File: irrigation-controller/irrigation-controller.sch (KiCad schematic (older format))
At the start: 12 parts, among them IC1 ATMEGA328-A_CHIPACCURATE, J1 B2B-I2C, P1 CONN_10, Q1 2N7002K, Q2 2N7002K, Q3 2N7002K, Q4 2N7002K

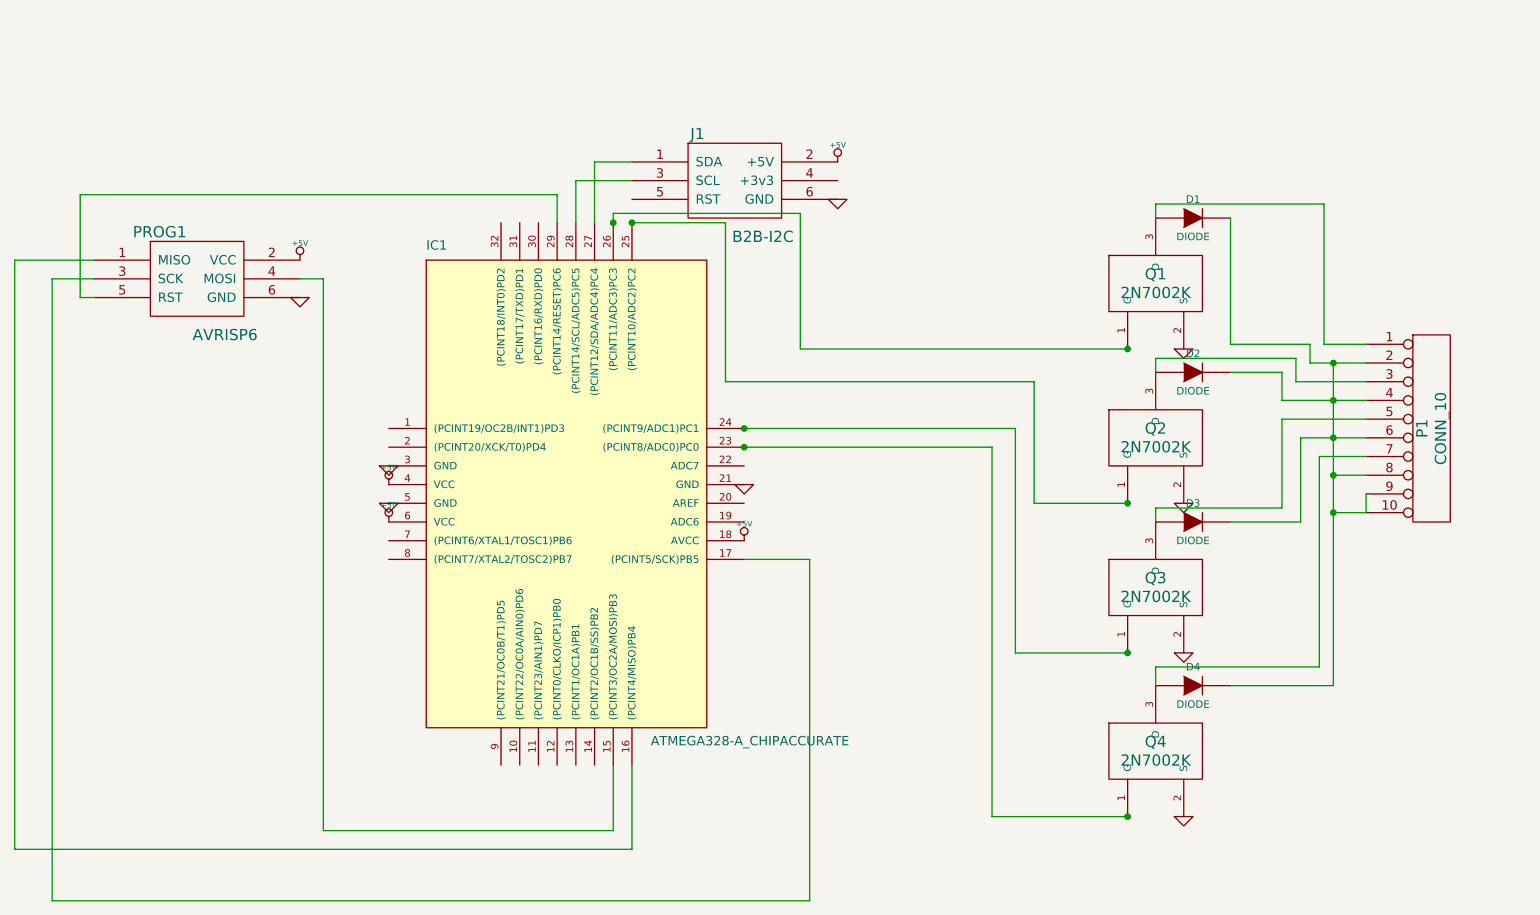
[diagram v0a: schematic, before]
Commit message: Add updated irrigation controller
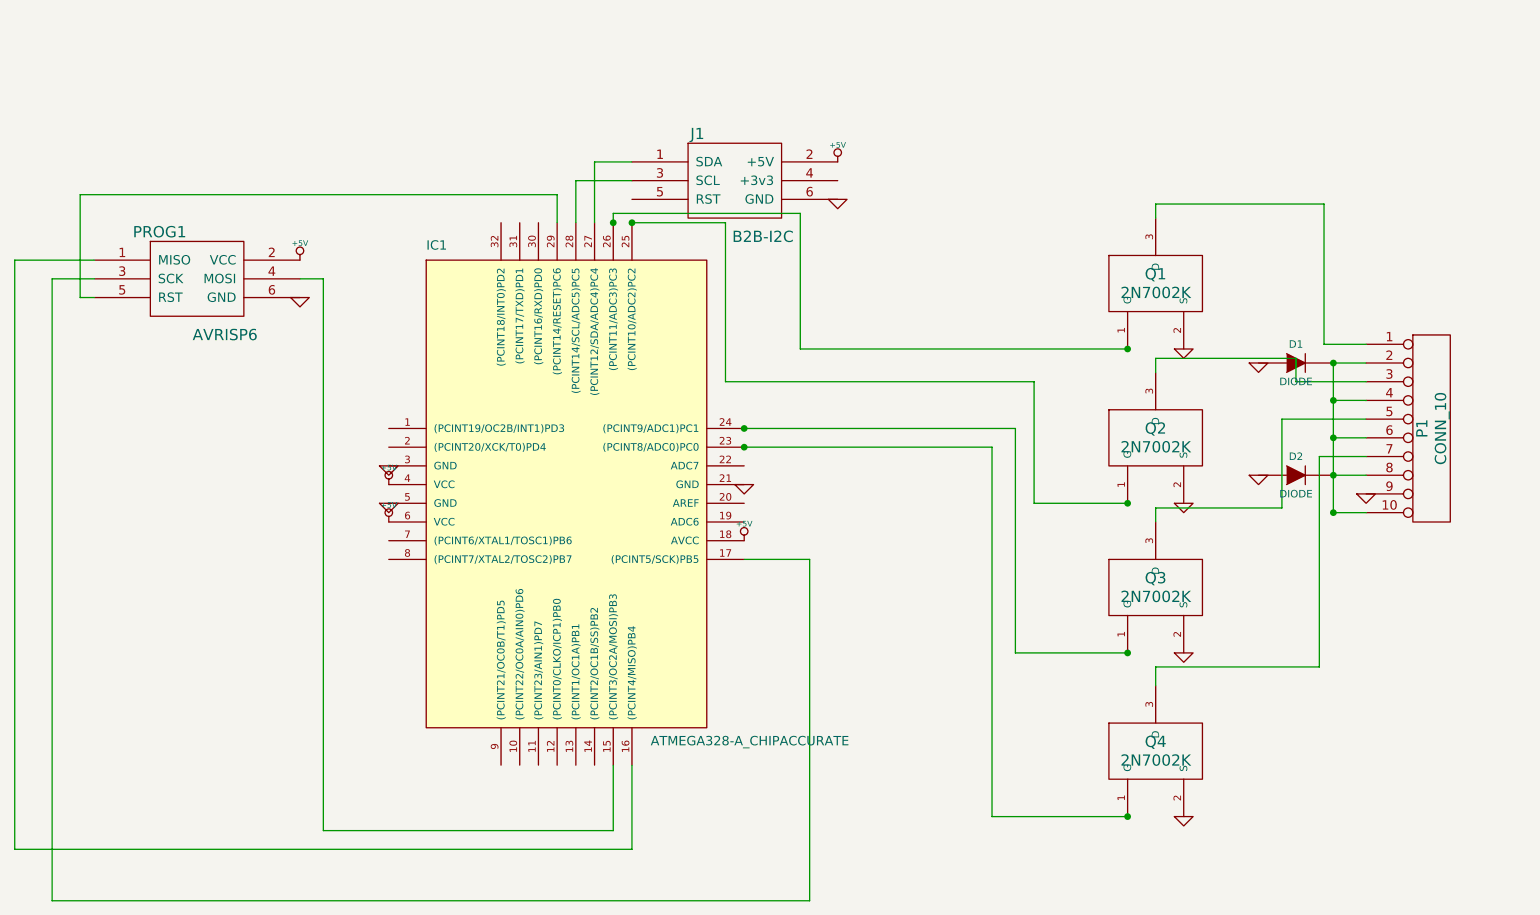
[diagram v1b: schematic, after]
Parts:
- removed D2, D3: DIODE, symbol DIODE
- renumbered D4 to D2
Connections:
- net GND: now also D1.1 (A), D2.1 (A), P1.9 (P9)
- net at P1.1 (P1), Q1.3 (D): no longer D1.1 (A)
- net at P1.7 (P7), Q4.3 (D): no longer D2.1 (A)
- net at D1.2 (K), D2.2 (K), P1.10 (P10)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: no longer P1.9 (P9)
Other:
- moved on the sheet: D1, D2

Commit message: Updated irrigation board: use Teensy or standard AVR-PoE board to drive FETs
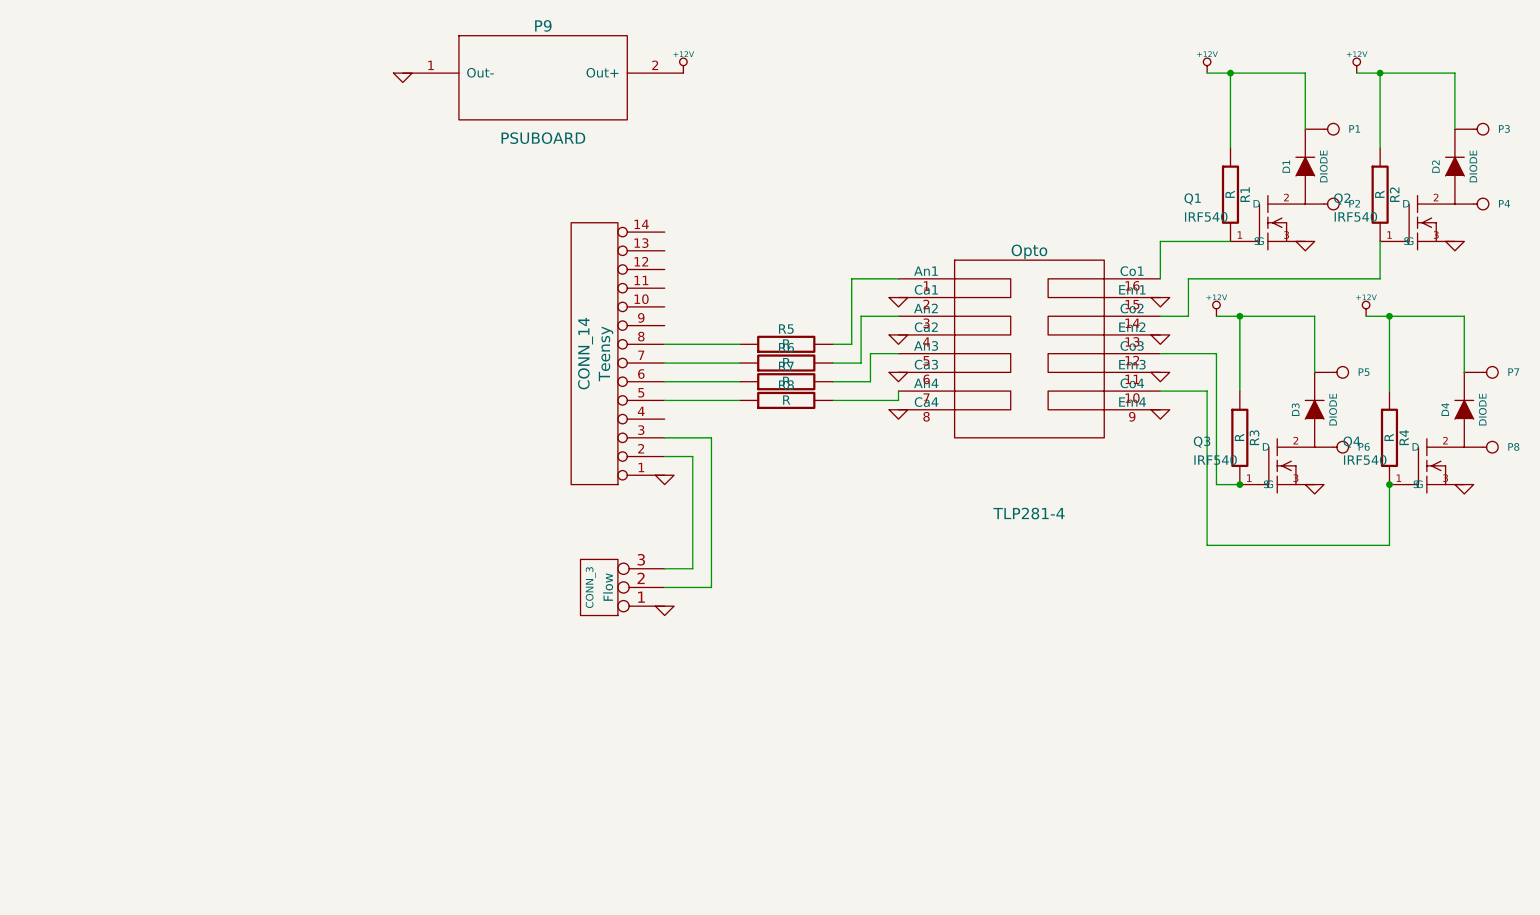
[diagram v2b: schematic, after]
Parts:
- removed IC1: ATMEGA328-A_CHIPACCURATE, TQFP32, symbol ATMEGA328-A_CHIPACCURATE
- removed J1: B2B-I2C, symbol B2B-I2C
- removed P1: CONN_10, symbol CONN_10
- removed PROG1: AVRISP6, symbol AVRISP6
- removed Q1, Q2, Q3, Q4: 2N7002K, symbol 2N7002K
- added D3, D4: DIODE, symbol DIODE
- added Flow: CONN_3, symbol CONN_3
- added Opto: TLP281-4, symbol TLP281-4
- added P1, P2, P3, P4, P5, P6, P7, P8: CONN_1, symbol CONN_1
- added P9: PSUBOARD, symbol PSUBOARD
- added Q1, Q2, Q3, Q4: IRF540, transistor-fet-TO220, symbol IRF540
- added R1, R2, R3, R4, R5, R6, R7, R8: R, symbol R
- added Teensy: CONN_14, symbol CONN_14
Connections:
- net GND: now also Flow.1 (P1), Opto.11 (Em3), Opto.13 (Em2), Opto.15 (Em1), Opto.2 (Ca1), Opto.4 (Ca2), Opto.6 (Ca3), Opto.8 (Ca4), Opto.9 (Em4), P9.1 (Out-), Q1.3 (S), Q2.3 (S), Q3.3 (S), Q4.3 (S), Teensy.1 (P1); no longer D1.1 (A), D2.1 (A)
- net +12V: now reaches D1.2 (K), D2.2 (K)
- net +12V: now also D3.2 (K), D4.2 (K), P1.1, P3.1, P5.1, P7.1, P9.2 (Out+), R1.1, R2.1, R3.1, R4.1
- new net: D1.1 (A), P2.1, Q1.2 (D)
- new net: Opto.16 (Co1), Q1.1 (G), R1.2
- new net: Opto.1 (An1), R5.2
- new net: Opto.10 (Co4), Q4.1 (G), R4.2
- new net: Opto.12 (Co3), Q3.1 (G), R3.2
- new net: Opto.14 (Co2), Q2.1 (G), R2.2
- new net: Opto.3 (An2), R6.2
- new net: Opto.5 (An3), R7.2
- new net: Opto.7 (An4), R8.2
- new net: D2.1 (A), P4.1, Q2.2 (D)
- new net: D4.1 (A), P8.1, Q4.2 (D)
- new net: D3.1 (A), P6.1, Q3.2 (D)
- new net: Flow.3 (P3), Teensy.2 (P2)
- new net: Flow.2 (PM), Teensy.3 (P3)
- new net: R8.1, Teensy.5 (P5)
- new net: R7.1, Teensy.6 (P6)
- new net: R6.1, Teensy.7 (P7)
- new net: R5.1, Teensy.8 (P8)

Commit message: Add power supply switching, and do some cleanup
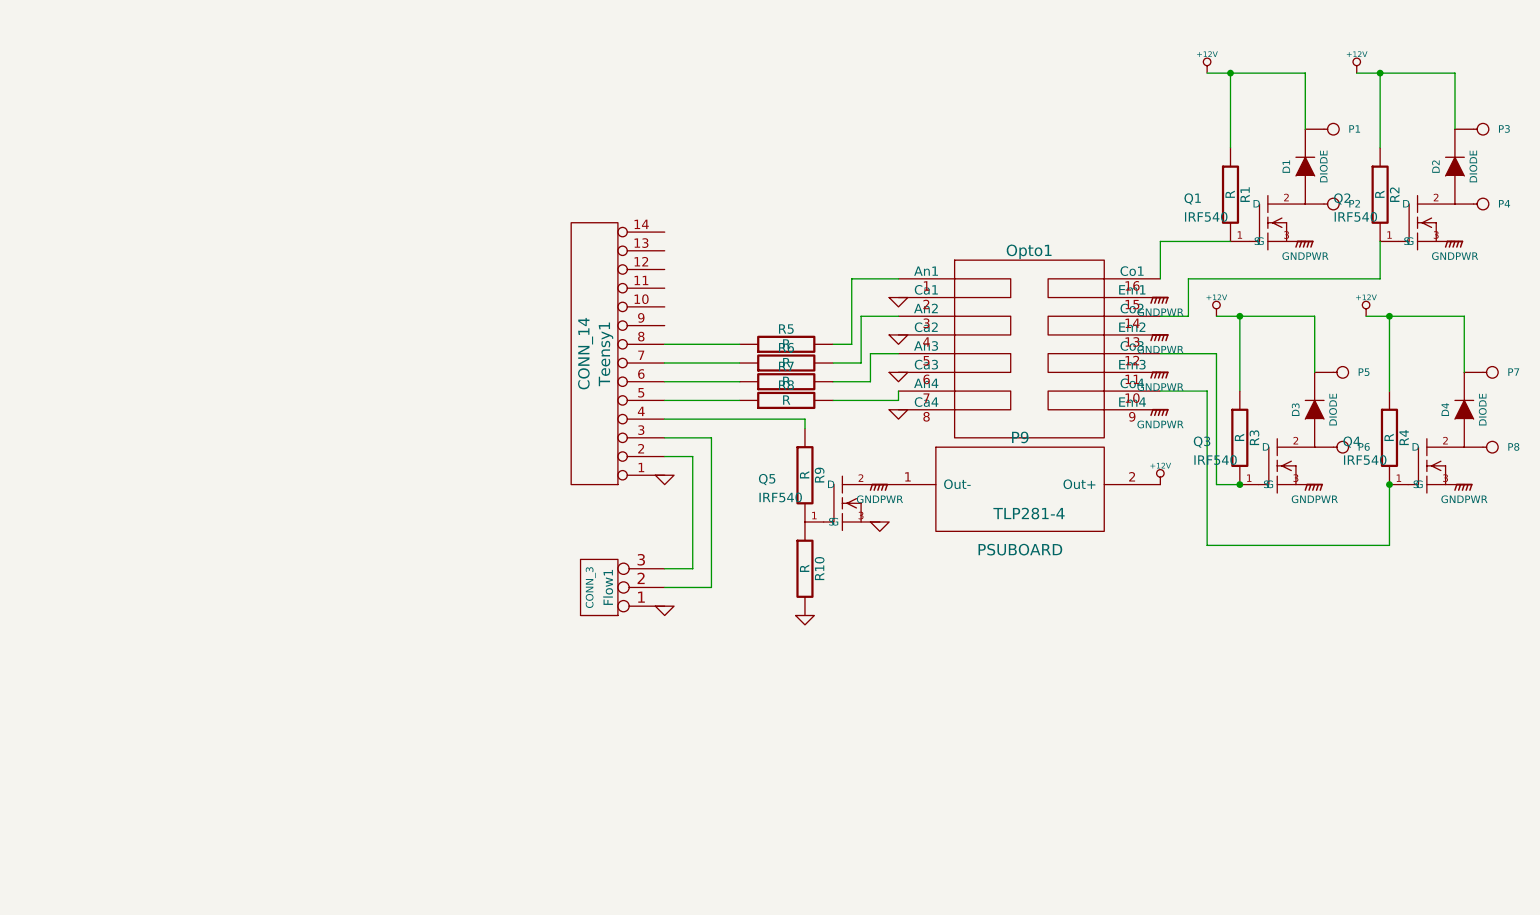
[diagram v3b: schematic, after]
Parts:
- added Q5: IRF540, transistor-fet-TO220, symbol IRF540
- added R10, R9: R, symbol R
- renumbered Flow to Flow1, Opto to Opto1, Teensy to Teensy1
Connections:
- net GND: now also Q5.3 (S), R10.2; no longer Opto1.11 (Em3), Opto1.13 (Em2), Opto1.15 (Em1), Opto1.9 (Em4), P9.1 (Out-), Q1.3 (S), Q2.3 (S), Q3.3 (S), Q4.3 (S)
- net at Teensy1.4 (P4): now also R9.1
- new net: Q5.1 (G), R10.1, R9.2
- new net GNDPWR: Opto1.11 (Em3), Opto1.13 (Em2), Opto1.15 (Em1), Opto1.9 (Em4), P9.1 (Out-), Q1.3 (S), Q2.3 (S), Q3.3 (S), Q4.3 (S), Q5.2 (D)
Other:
- moved on the sheet: P9
